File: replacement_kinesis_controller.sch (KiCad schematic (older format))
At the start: 41 parts

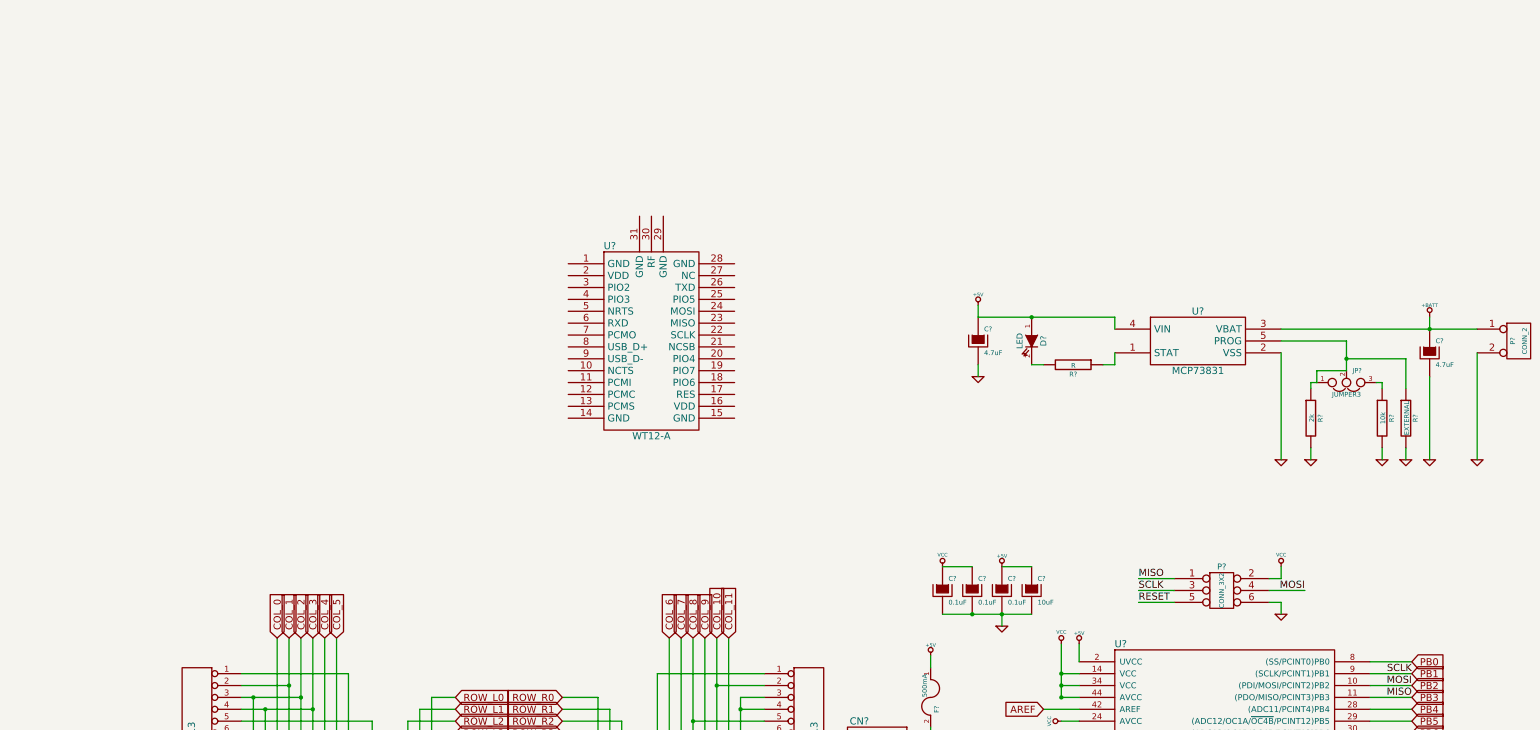
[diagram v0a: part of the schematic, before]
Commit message: Add all bluetooth headers
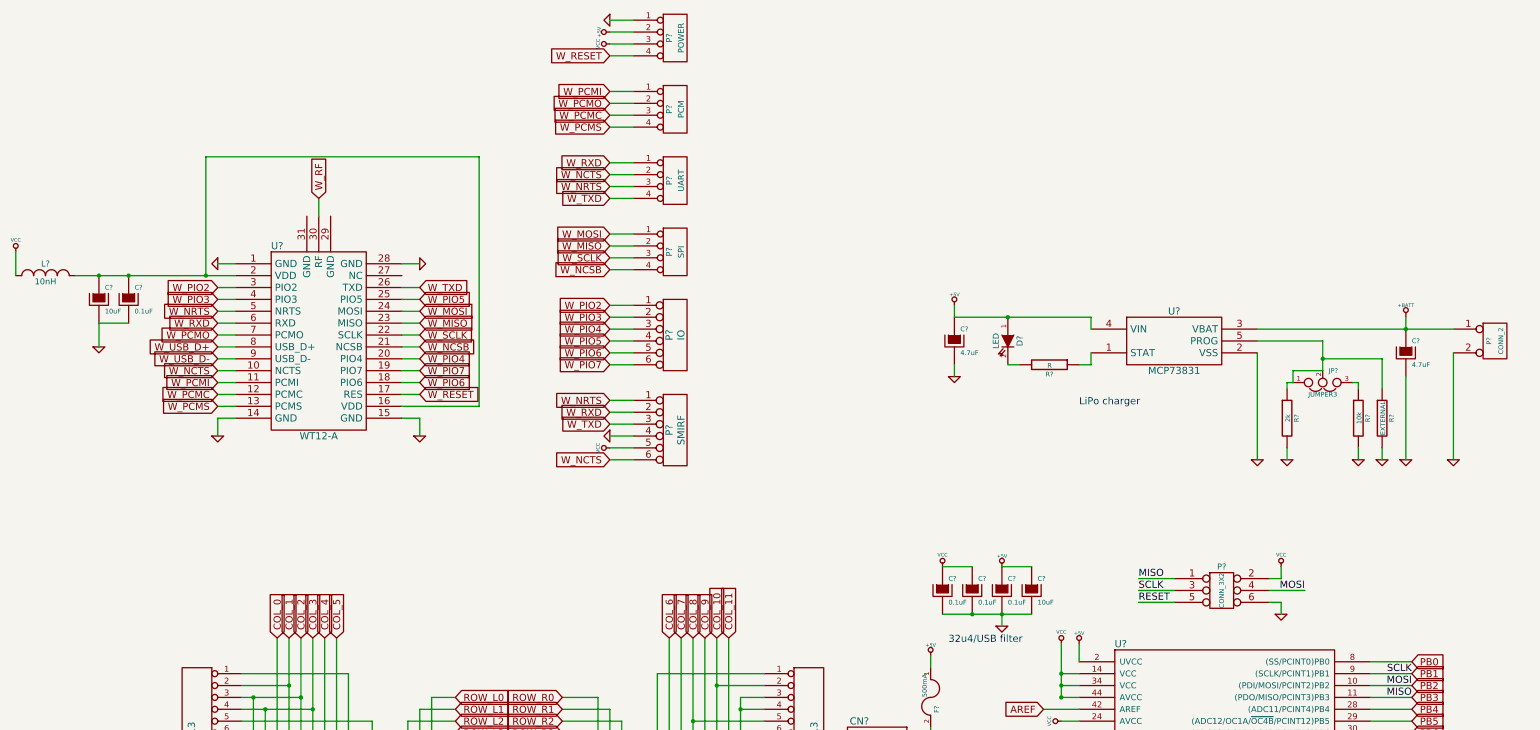
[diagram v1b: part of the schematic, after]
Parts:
- added C?: 10uF, symbol CP
- added C?: 0.1uF, symbol CP
- added L?: 10nH, symbol INDUCTOR_SMALL
- added P?: SMIRF, symbol CONN_6
- added P?: IO, symbol CONN_6
- added P?: SPI, symbol CONN_4
- added P?: UART, symbol CONN_4
- added P?: PCM, symbol CONN_4
- added P?: POWER, symbol CONN_4
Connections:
- net +5V: now also P?.2 (P2)
- net GND: now also U?.1 (GND), U?.14 (GND), U?.15 (GND), U?.28 (GND), C?.2, C?.2, P?.1 (P1), P?.4
- net VCC: now also L?.1, P?.3 (P3), P?.5
- net W_NCTS: now reaches U?.10 (NCTS)
- net W_NCTS: now also P?.2 (P2), P?.6
- net W_PCMI: now reaches U?.11 (PCMI)
- net W_PCMI: now also P?.1 (P1)
- net W_PCMC: now reaches U?.12 (PCMC)
- net W_PCMC: now also P?.3 (P3)
- net W_PCMS: now reaches U?.13 (PCMS)
- net W_PCMS: now also P?.4 (P4)
- net at U?.16 (VDD): now also U?.2 (VDD), C?.1, C?.1, L?.2
- net W_RESET: now reaches U?.17 (RES)
- net W_RESET: now also P?.4 (P4)
- net W_PIO6: now reaches U?.18 (PIO6)
- net W_PIO6: now also P?.5
- net W_PIO7: now reaches U?.19 (PIO7)
- net W_PIO7: now also P?.6
- net W_PIO4: now reaches U?.20 (PIO4)
- net W_PIO4: now also P?.3
- net W_NCSB: now reaches U?.21 (NCSB)
- net W_NCSB: now also P?.4 (P4)
- net W_SCLK: now reaches U?.22 (SCLK)
- net W_SCLK: now also P?.3 (P3)
- net W_MISO: now reaches U?.23 (MISO)
- net W_MISO: now also P?.2 (P2)
- net W_MOSI: now reaches U?.24 (MOSI)
- net W_MOSI: now also P?.1 (P1)
- net W_PIO5: now reaches U?.25 (PIO5)
- net W_PIO5: now also P?.4
- net W_TXD: now reaches U?.26 (TXD)
- net W_TXD: now also P?.3, P?.4 (P4)
- net W_PIO2: now reaches U?.3 (PIO2)
- net W_PIO2: now also P?.1
- net W_RF: now reaches U?.30 (RF)
- net W_PIO3: now reaches U?.4 (PIO3)
- net W_PIO3: now also P?.2
- net W_NRTS: now reaches U?.5 (NRTS)
- net W_NRTS: now also P?.1, P?.3 (P3)
- net W_RXD: now reaches U?.6 (RXD)
- net W_RXD: now also P?.1 (P1), P?.2
- net W_PCMO: now reaches U?.7 (PCMO)
- net W_PCMO: now also P?.2 (P2)
- net W_USB_D+: now reaches U?.8 (USB_D+)
- net W_USB_D-: now reaches U?.9 (USB_D-)
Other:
- note added: "32u4/USB filter"
- note added: "LiPo charger"
- moved on the sheet: C?, D?, JP?, P?, R?, U?

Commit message: More stuff, including LEDs
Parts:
- added U? (x4): WS2811_RGB_LED, symbol WS2811_RGB_LED
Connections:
- net GND: now also U?.6 (VSS), U?.6 (VSS), U?.6 (VSS), U?.6 (VSS)
- net VCC: now also U?.3 (VCC), U?.3 (VCC), U?.3 (VCC), U?.3 (VCC), U?.5 (VDD), U?.5 (VDD), U?.5 (VDD), U?.5 (VDD)
- new net: U?.1 (DO), U?.2 (DI) (x3)
- new net LED_DATA: U?.2 (DI)
- new net LED_OUT: U?.1 (DO)

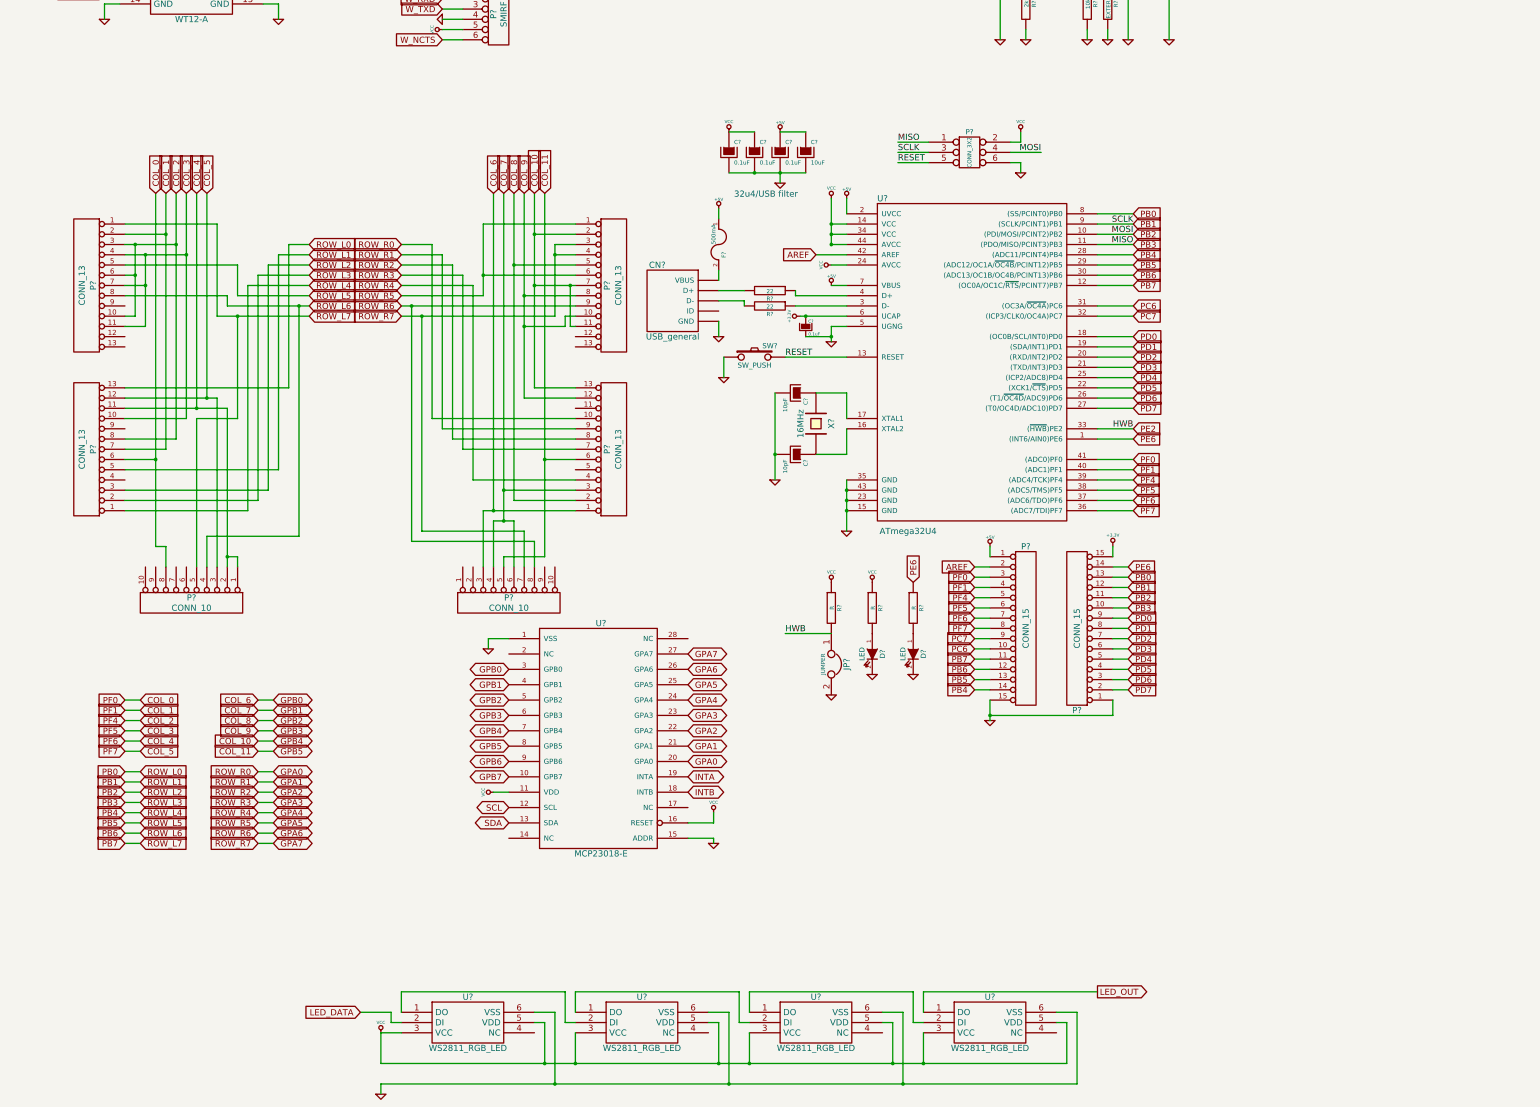
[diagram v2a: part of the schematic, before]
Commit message: Add some connections and many headers
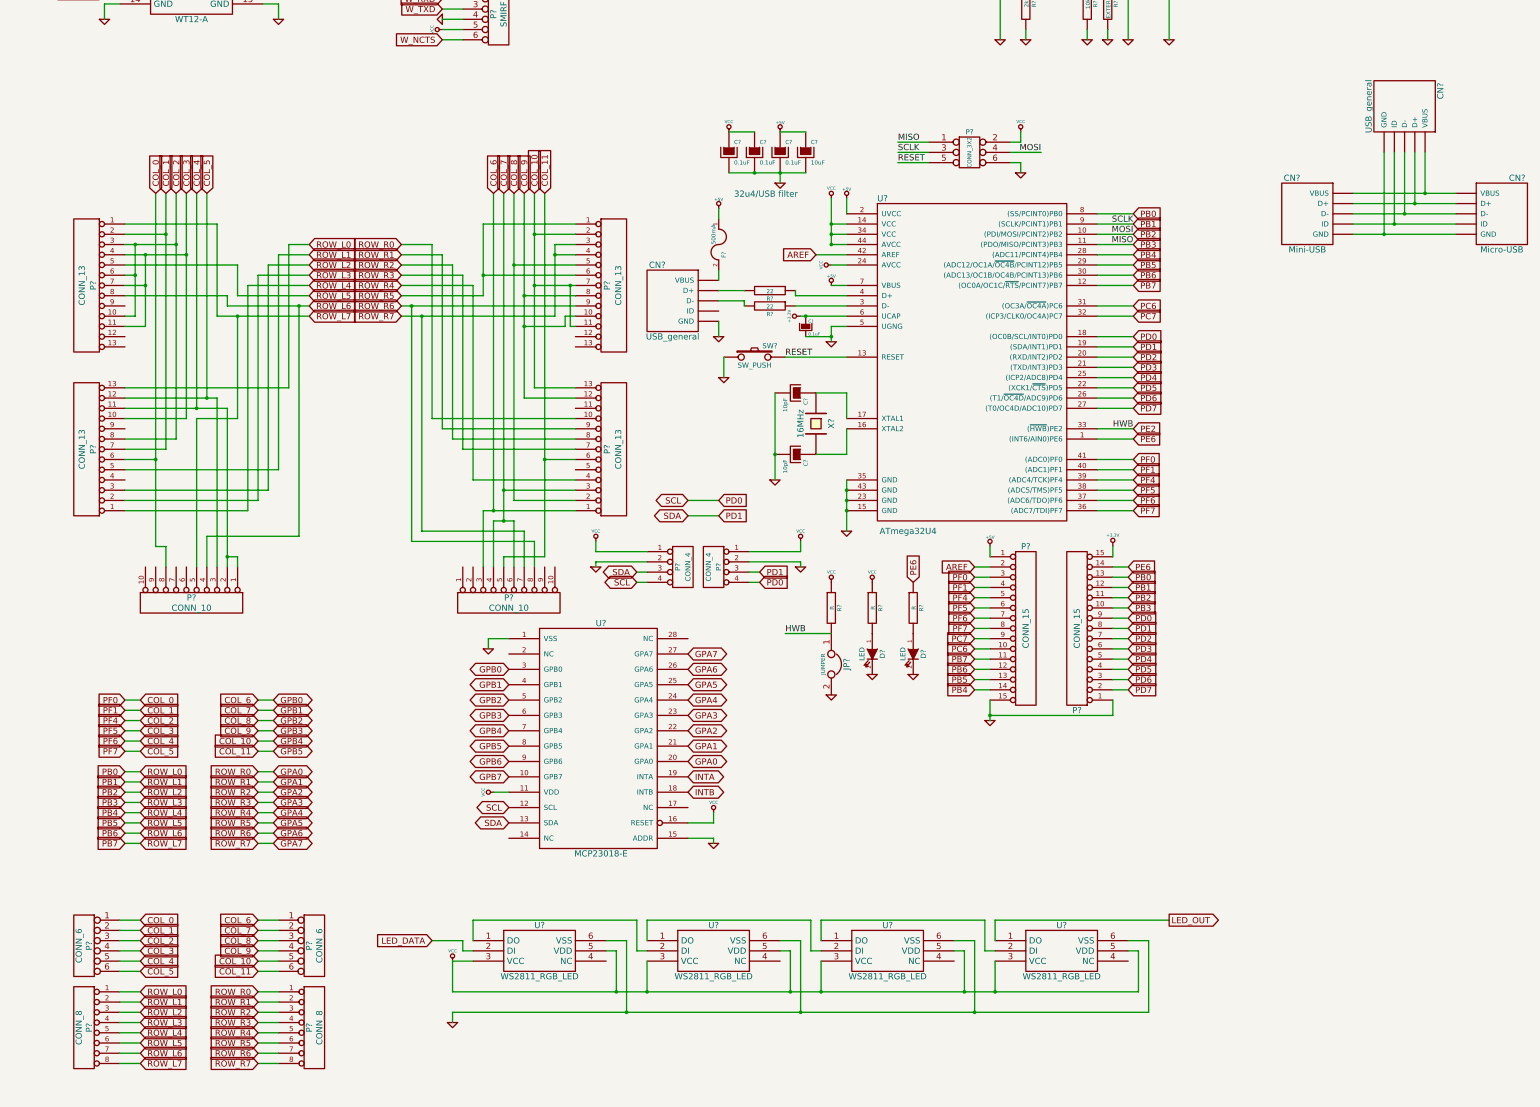
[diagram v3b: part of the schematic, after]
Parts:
- added CN?: Mini-USB, symbol USB_general
- added CN?: USB_general, symbol USB_general
- added CN?: Micro-USB, symbol USB_general
- added P? (x2): CONN_6, symbol CONN_6
- added P? (x2): CONN_8, symbol CONN_8
- added P? (x2): CONN_4, symbol CONN_4
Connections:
- net SCL is gone; now on net PD0: U?.12 (SCL)
- net SDA is gone; now on net PD1: U?.13 (SDA)
- net COL_0: now also P?.1
- net COL_1: now also P?.2
- net COL_10: now also P?.5
- net COL_11: now also P?.6
- net COL_2: now also P?.3
- net COL_3: now also P?.4
- net COL_4: now also P?.5
- net COL_5: now also P?.6
- net COL_6: now also P?.1
- net COL_7: now also P?.2
- net COL_8: now also P?.3
- net COL_9: now also P?.4
- net GND: now also P?.2 (P2), P?.2 (P2)
- net GPA0: now also P?.1 (P1)
- net GPA1: now also P?.2 (P2)
- net GPA2: now also P?.3 (P3)
- net GPA3: now also P?.4 (P4)
- net GPA4: now also P?.5 (P5)
- net GPA5: now also P?.6 (P6)
- net GPA6: now also P?.7 (P7)
- net GPA7: now also P?.8 (P8)
- net PB0: now also P?.1 (P1)
- net PB1: now also P?.2 (P2)
- net PB2: now also P?.3 (P3)
- net PB3: now also P?.4 (P4)
- net PB4: now also P?.5 (P5)
- net PB5: now also P?.6 (P6)
- net PB6: now also P?.7 (P7)
- net PB7: now also P?.8 (P8)
- net PD0: now also P?.4 (P4), P?.4 (P4)
- net PD1: now also P?.3 (P3), P?.3 (P3)
- net VCC: now also P?.1 (P1), P?.1 (P1)
- new net: CN?.~ (VBUS), CN?.~ (VBUS), CN?.~ (VBUS) (x5)
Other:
- moved on the sheet: U?

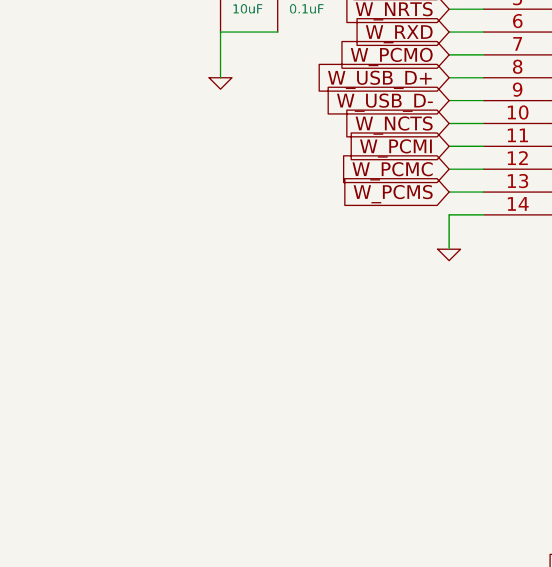
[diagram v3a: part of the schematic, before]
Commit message: Connect ATmega to WT12
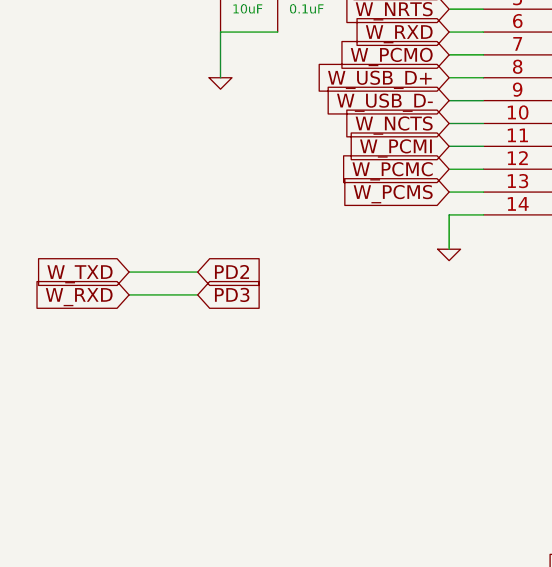
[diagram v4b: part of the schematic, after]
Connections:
- net W_RXD is gone; now on net PD3: P?.1 (P1), P?.2, U?.6 (RXD)
- net W_TXD is gone; now on net PD2: P?.3, P?.4 (P4), U?.26 (TXD)
- new net: CN?.~ (VBUS), CN?.~ (VBUS), CN?.~ (VBUS) (x4)
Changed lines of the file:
@@
 	13700 900  13700 1300
 Connection ~ 13700 1300
+Text GLabel -300 -300 2    60   Input ~ 0
+PD2
+Text GLabel -300 -200 2    60   Input ~ 0
+PD3
+Text GLabel -600 -300 0    60   Input ~ 0
+W_TXD
+Text GLabel -600 -200 0    60   Input ~ 0
+W_RXD
+Wire Wire Line
+	-600 -300 -300 -300
+Wire Wire Line
+	-600 -200 -300 -200
 $EndSCHEMATC
